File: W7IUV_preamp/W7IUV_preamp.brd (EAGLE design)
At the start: 60.3 x 36.5 mm, 30 parts, among them K1 G5L, Q1 2N2219A

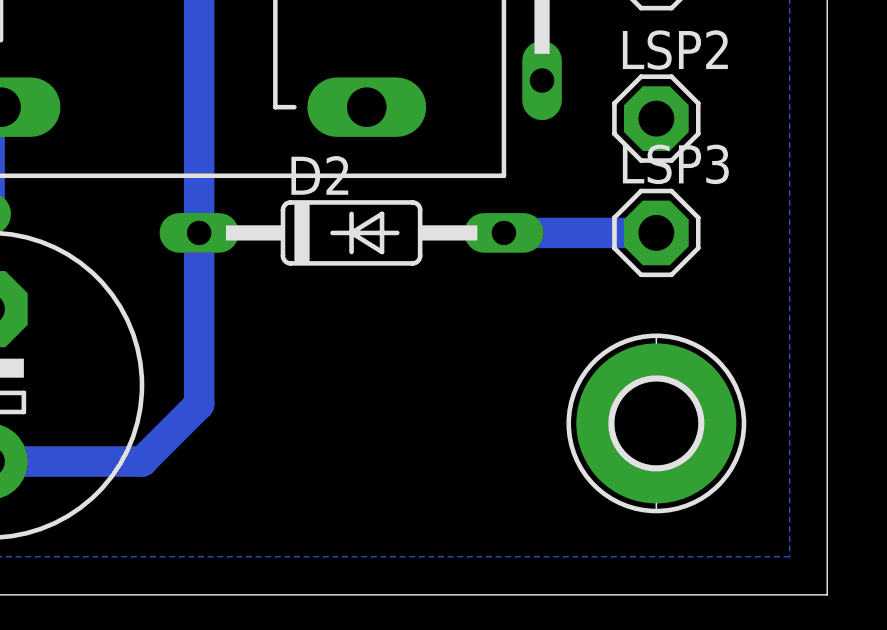
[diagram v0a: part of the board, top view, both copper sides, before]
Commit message: Adding bypass cap
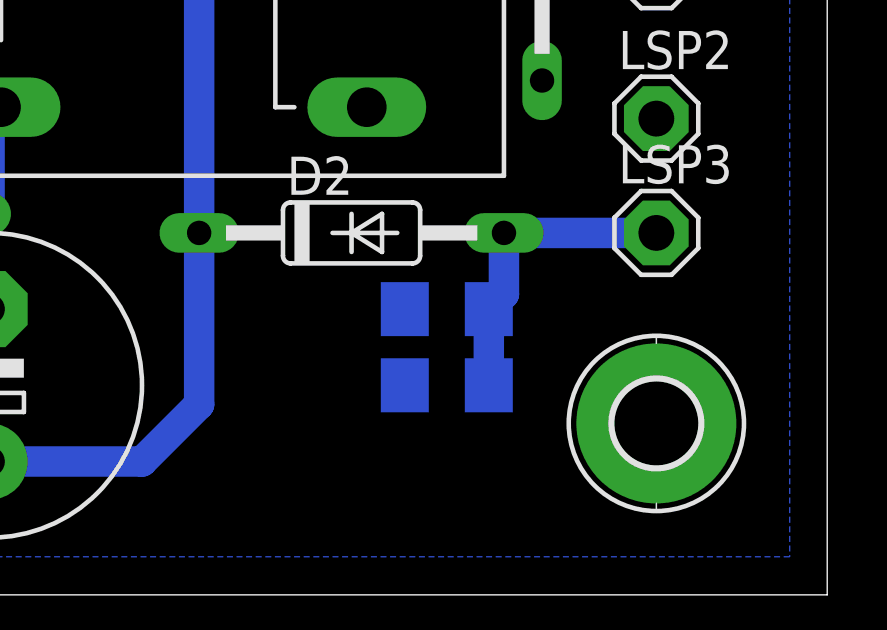
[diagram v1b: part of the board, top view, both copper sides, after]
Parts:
- added C8, C9: (no value), rcl:C1206
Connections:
- net GND: now also C8.2, C9.2
- net N$11: now also C8.1, C9.1
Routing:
- net N$11: track 5.08 -> 10.4 mm
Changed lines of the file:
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@@
 <element name="R4" library="rcl" package="M1206" value="" x="20.955" y="25.4" rot="MR90"/>
 <element name="R5" library="rcl" package="M1206" value="" x="20.955" y="30.48" rot="MR90"/>
+<element name="C8" library="rcl" package="C1206" value="" x="47.625" y="9.525" rot="MR0"/>
+<element name="C9" library="rcl" package="C1206" value="" x="47.625" y="6.985" rot="MR0"/>
 </elements>
 <signals>
@@
 </polygon>
 <contactref element="R5" pad="2"/>
+<contactref element="C9" pad="2"/>
+<contactref element="C8" pad="2"/>
 </signal>
 <signal name="N$2">
@@
 <contactref element="LSP3" pad="MP"/>
 <wire x1="54.61" y1="12.065" x2="49.53" y2="12.065" width="1.016" layer="16"/>
+<contactref element="C9" pad="1"/>
+<contactref element="C8" pad="1"/>
+<wire x1="49.53" y1="12.065" x2="49.53" y2="10.03" width="1.016" layer="16"/>
+<wire x1="49.53" y1="10.03" x2="49.025" y2="9.525" width="1.016" layer="16"/>
+<wire x1="49.025" y1="9.525" x2="49.025" y2="6.985" width="1.016" layer="16"/>
 </signal>
 <signal name="N$1">
